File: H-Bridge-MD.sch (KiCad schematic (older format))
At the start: 69 parts, among them IC1 SI8650AB-B-IS1, IC2 A3921KLPTR-T, IC3 SI8650AB-B-IS1, IC4 A3921KLPTR-T, J1 Conn_01x02, J2 Conn_01x03, J3 Conn_01x05, J4 Conn_01x02, J5 Bus_mechaken_PCIexpress_x16_1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, Q1 NVMFD5C446NT1G, Q2 NVMFD5C446NT1G, Q3 NVMFD5C446NT1G, Q4 NVMFD5C446NT1G, U1 LDL1117S33R_SOT223-4, U2 STM32F042K6Tx, U3 MCP2562-E-SN, U4 LDL1117S33TR_SOT223-4

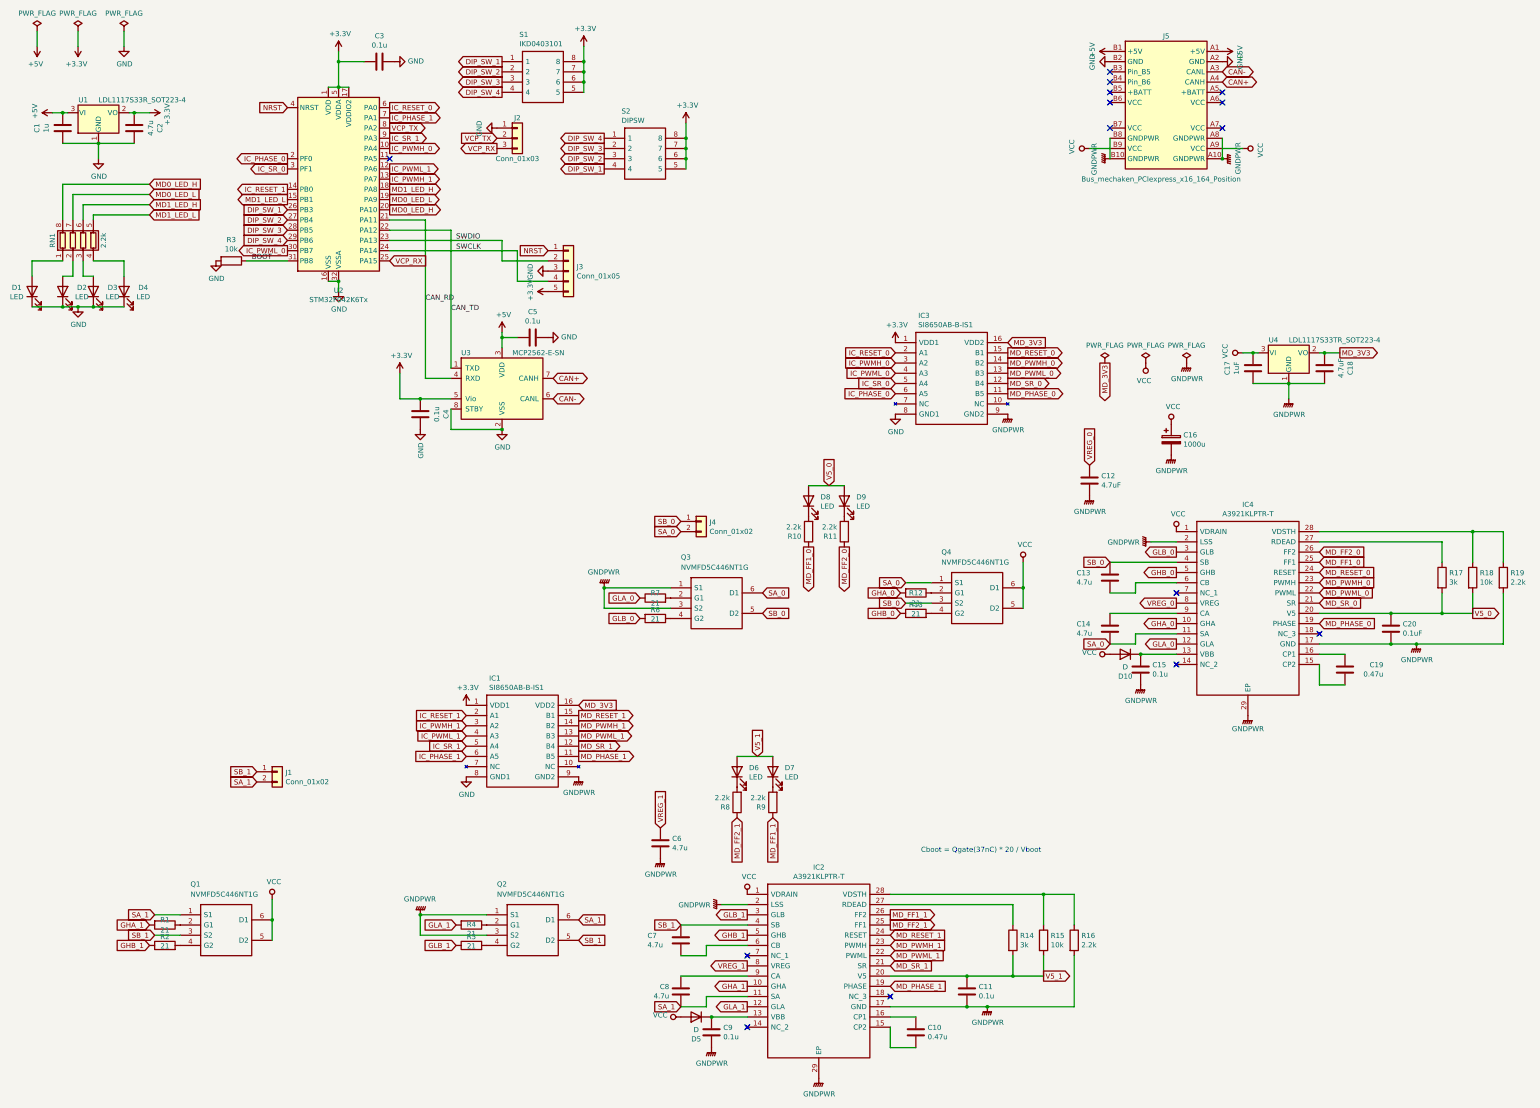
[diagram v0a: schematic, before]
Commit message: change
電源部のパスコンの追加
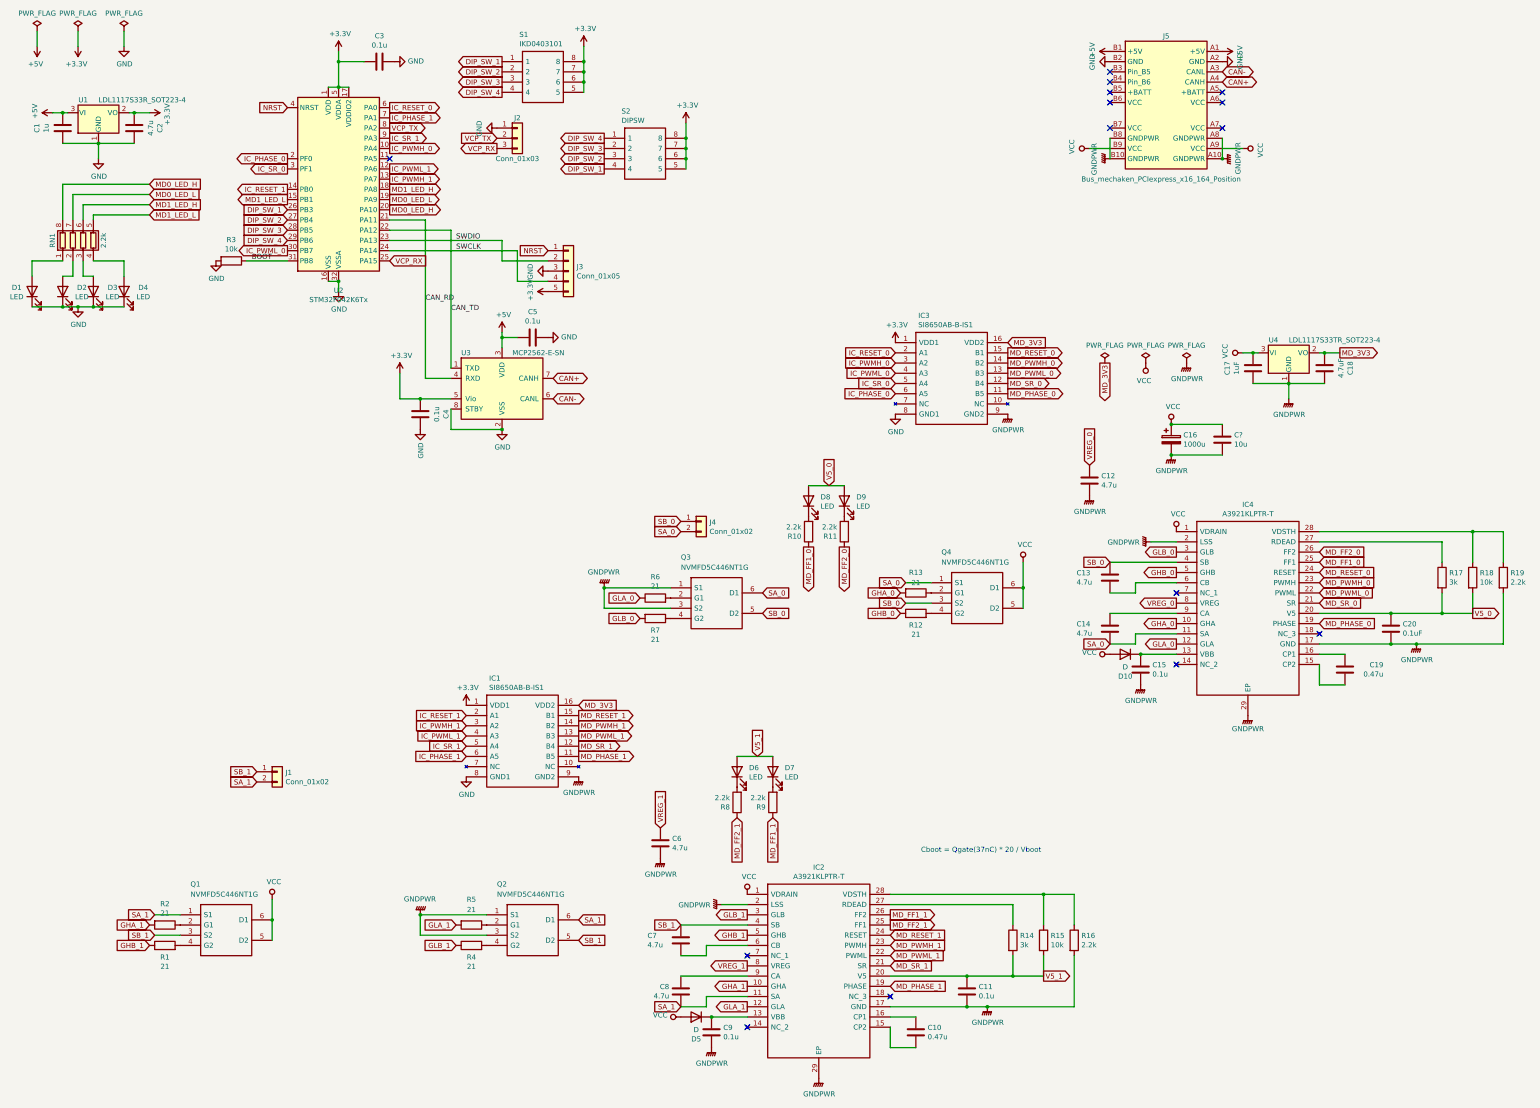
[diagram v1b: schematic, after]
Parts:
- added C?: 10u, Capacitor_SMD:C_0805_2012Metric, symbol Device:C
- C12: value 4.7uF -> 4.7u
- D10: footprint LED_SMD:LED_0603_1608Metric_Castellated -> Diode_SMD:D_0603_1608Metric
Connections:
- net GNDPWR: now also C?.2
- net VCC: now also C?.1
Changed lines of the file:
@@
 F 0 "D10" H 11400 7166 50  0000 C CNN
 F 1 "D" H 11400 7075 50  0000 C CNN
-F 2 "LED_SMD:LED_0603_1608Metric_Castellated" H 11400 6950 50  0001 C CNN
+F 2 "Diode_SMD:D_0603_1608Metric" H 11400 6950 50  0001 C CNN
 F 3 "~" H 11400 6950 50  0001 C CNN
 	1    11400 6950
@@
 U 1 1 5DA97C08
 P 2000 9600
-F 0 "R2" V 2115 9600 50  0000 C CNN
-F 1 "21" V 2206 9600 50  0000 C CNN
+F 0 "R2" V 1793 9600 50  0000 C CNN
+F 1 "21" V 1884 9600 50  0000 C CNN
 F 2 "Resistor_SMD:R_0603_1608Metric" V 1930 9600 50  0001 C CNN
 F 3 "~" H 2000 9600 50  0001 C CNN
@@
 U 1 1 5DA97BF0
 P 2000 9800
-F 0 "R1" V 2250 9800 50  0000 C CNN
-F 1 "21" V 2150 9800 50  0000 C CNN
+F 0 "R1" V 1885 9800 50  0000 C CNN
+F 1 "21" V 1794 9800 50  0000 C CNN
 F 2 "Resistor_SMD:R_0603_1608Metric" V 1930 9800 50  0001 C CNN
 F 3 "~" H 2000 9800 50  0001 C CNN
@@
 U 1 1 5DC02421
 P 9350 6550
-F 0 "R12" V 9550 6550 50  0000 C CNN
-F 1 "21" V 9450 6550 50  0000 C CNN
+F 0 "R12" V 9235 6550 50  0000 C CNN
+F 1 "21" V 9144 6550 50  0000 C CNN
 F 2 "Resistor_SMD:R_0603_1608Metric" V 9280 6550 50  0001 C CNN
 F 3 "~" H 9350 6550 50  0001 C CNN
@@
 U 1 1 5DC02427
 P 9350 6350
-F 0 "R13" V 9465 6350 50  0000 C CNN
-F 1 "21" V 9556 6350 50  0000 C CNN
+F 0 "R13" V 9150 6350 50  0000 C CNN
+F 1 "21" V 9250 6350 50  0000 C CNN
 F 2 "Resistor_SMD:R_0603_1608Metric" V 9280 6350 50  0001 C CNN
 F 3 "~" H 9350 6350 50  0001 C CNN
@@
 P 11050 5250
 F 0 "C12" H 11165 5296 50  0000 L CNN
-F 1 "4.7uF" H 11165 5205 50  0000 L CNN
+F 1 "4.7u" H 11165 5205 50  0000 L CNN
 F 2 "Capacitor_SMD:C_0805_2012Metric" H 11088 5100 50  0001 C CNN
 F 3 "~" H 11050 5250 50  0001 C CNN
@@
 U 1 1 5DC02488
 P 6800 6600
-F 0 "R7" V 6550 6600 50  0000 C CNN
-F 1 "21" V 6650 6600 50  0000 C CNN
+F 0 "R7" V 6915 6600 50  0000 C CNN
+F 1 "21" V 7006 6600 50  0000 C CNN
 F 2 "Resistor_SMD:R_0603_1608Metric" V 6730 6600 50  0001 C CNN
 F 3 "~" H 6800 6600 50  0001 C CNN
@@
 U 1 1 5DC0241B
 P 6800 6400
-F 0 "R6" V 6685 6400 50  0000 C CNN
-F 1 "21" V 6594 6400 50  0000 C CNN
+F 0 "R6" V 7007 6400 50  0000 C CNN
+F 1 "21" V 6916 6400 50  0000 C CNN
 F 2 "Resistor_SMD:R_0603_1608Metric" V 6730 6400 50  0001 C CNN
 F 3 "~" H 6800 6400 50  0001 C CNN
@@
 U 1 1 5DA97C02
 P 5000 9600
-F 0 "R5" V 5115 9600 50  0000 C CNN
-F 1 "21" V 5206 9600 50  0000 C CNN
+F 0 "R5" V 4750 9600 50  0000 C CNN
+F 1 "21" V 4850 9600 50  0000 C CNN
 F 2 "Resistor_SMD:R_0603_1608Metric" V 4930 9600 50  0001 C CNN
 F 3 "~" H 5000 9600 50  0001 C CNN
@@
 U 1 1 5DA97BEA
 P 5000 9800
-F 0 "R4" V 5207 9800 50  0000 C CNN
-F 1 "21" V 5116 9800 50  0000 C CNN
+F 0 "R4" V 4885 9800 50  0000 C CNN
+F 1 "21" V 4794 9800 50  0000 C CNN
 F 2 "Resistor_SMD:R_0603_1608Metric" V 4930 9800 50  0001 C CNN
 F 3 "~" H 5000 9800 50  0001 C CNN
@@
 	0    -1   -1   0
 $EndComp
+$Comp
+L Device:C C?
+U 1 1 5E1E4833
+P 12350 4850
+F 0 "C?" H 12465 4896 50  0000 L CNN
+F 1 "10u" H 12465 4805 50  0000 L CNN
+F 2 "Capacitor_SMD:C_0805_2012Metric" H 12388 4700 50  0001 C CNN
+F 3 "~" H 12350 4850 50  0001 C CNN
+	1    12350 4850
+	1    0    0    -1
+$EndComp
+Wire Wire Line
+	11850 4700 12350 4700
+Connection ~ 11850 4700
+Wire Wire Line
+	11850 5000 12350 5000
+Connection ~ 11850 5000
 $EndSCHEMATC

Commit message: fix
Motor0側にあるA3921のVCCにつながるビアを増加
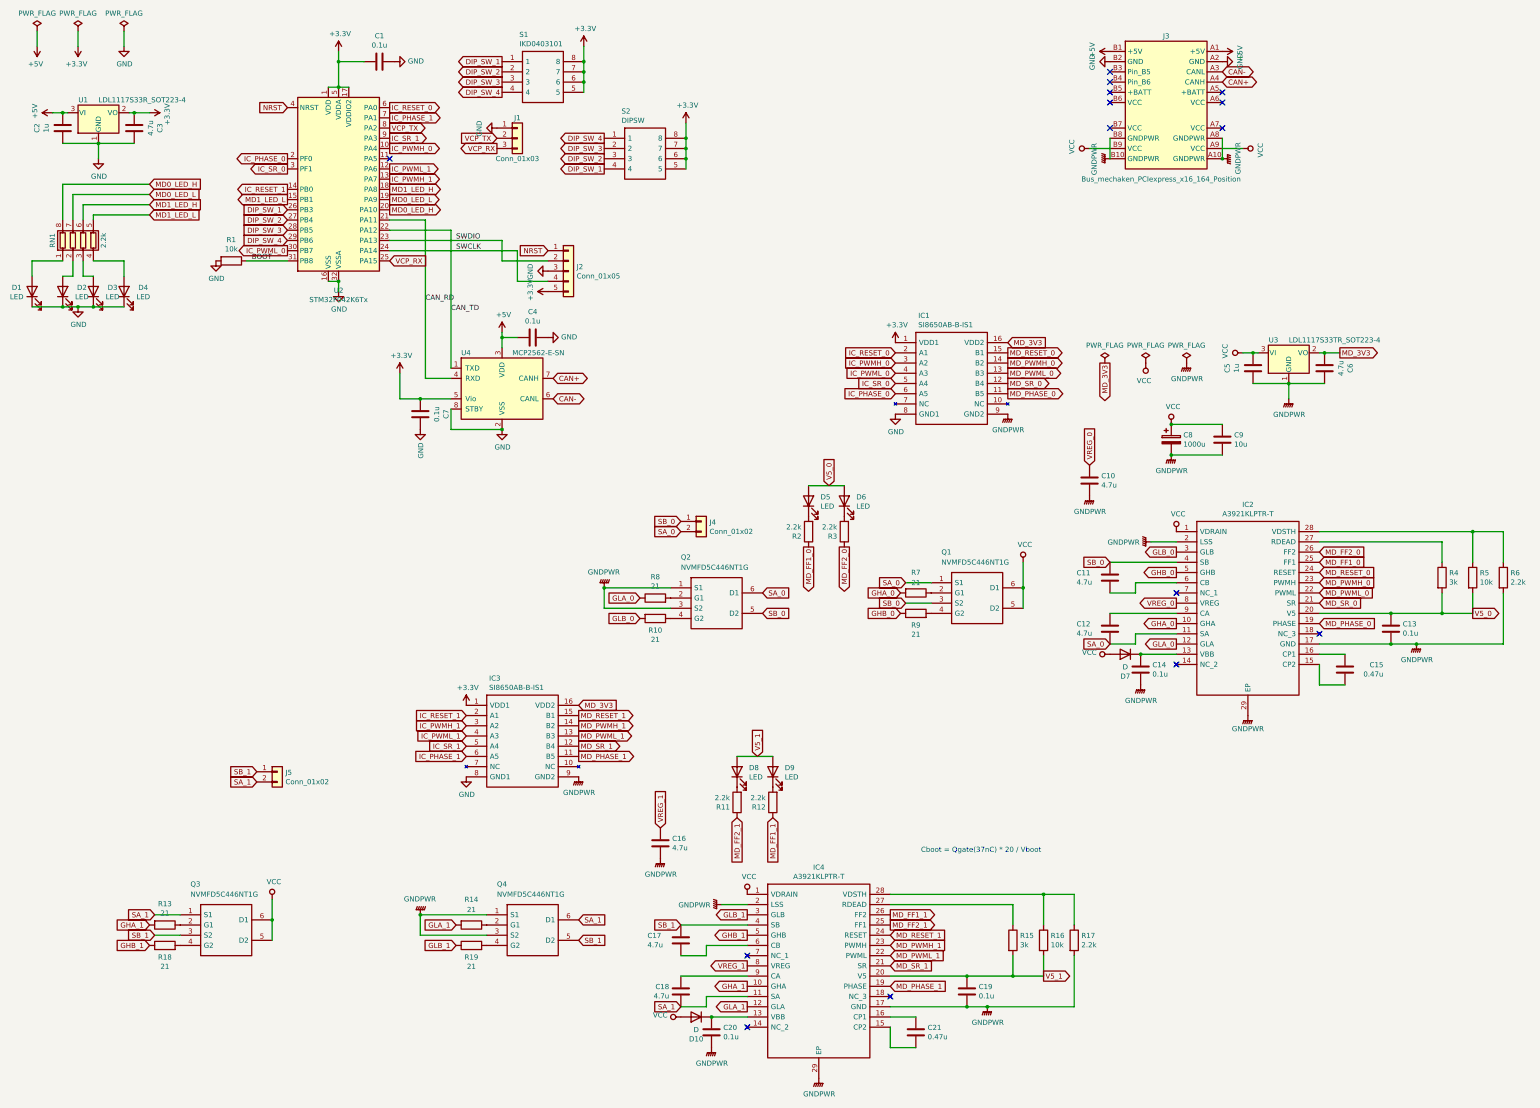
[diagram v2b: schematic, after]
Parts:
- C13: renamed from C20; value 0.1uF -> 0.1u
- C5: renamed from C17; value 1uF -> 1u
- C6: renamed from C18; value 4.7uF -> 4.7u
- gave numbers to parts that had none: 1
- renumbered C3 to C1, C12 to C10, C13 to C11, C14 to C12, C15 to C14, C19 to C15, C6 to C16, C7 to C17, C8 to C18, C11 to C19, C1 to C2, C9 to C20, C10 to C21, C2 to C3, C5 to C4, C4 to C7, C16 to C8, D5 to D10, D8 to D5, D9 to D6, D10 to D7, D6 to D8, D7 to D9, IC3 to IC1, IC4 to IC2, IC1 to IC3, IC2 to IC4, J2 to J1, J3 to J2, J5 to J3, J1 to J5, Q4 to Q1, Q3 to Q2, Q1 to Q3, Q2 to Q4, R3 to R1, R7 to R10, R8 to R11, R9 to R12, R2 to R13, R5 to R14, R14 to R15, R15 to R16, R16 to R17, R1 to R18, R4 to R19, R10 to R2, R11 to R3, R17 to R4, R18 to R5, R19 to R6, R13 to R7, R6 to R8, R12 to R9, U4 to U3, U3 to U4

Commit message: change LDO
アイソレータ用のLDOを変更
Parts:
- removed U3: LDL1117S33TR_SOT223-4, Package_TO_SOT_SMD:SOT-223-3_TabPin2, symbol H-Bridge-MD-rescue:LD1117S33TR_SOT223-Regulator_Linear
- added IC2: AP7381-50SA-7, SOT96P240X105-3N, symbol SamacSys_Parts:AP7381-50SA-7
- C6: value 4.7u -> 2.2u
- renumbered IC2 to IC3, IC3 to IC4, IC4 to IC5, U4 to U3
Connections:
- net GNDPWR: now also IC2.3 (GND)
- net MD_3V3: now also IC2.2 (VOUT)
- net VCC: now also IC2.1 (VIN)
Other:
- moved on the sheet: C5, C6
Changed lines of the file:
@@
 NoConn ~ 11900 7050
 $Comp
-L SamacSys_Parts:A3921KLPTR-T IC2
+L SamacSys_Parts:A3921KLPTR-T IC3
 U 1 1 5DC023BF
 P 11900 5750
-F 0 "IC2" H 12600 6015 50  0000 C CNN
+F 0 "IC3" H 12600 6015 50  0000 C CNN
 F 1 "A3921KLPTR-T" H 12600 5924 50  0000 C CNN
 F 2 "SamacSys_Parts:SOP65P640X120-29N" H 13150 5850 50  0001 L CNN
@@
 $EndComp
 $Comp
-L SamacSys_Parts:SI8650AB-B-IS1 IC3
+L SamacSys_Parts:SI8650AB-B-IS1 IC4
 U 1 1 5DAFE258
 P 4950 7450
-F 0 "IC3" H 5173 7715 50  0000 L CNN
+F 0 "IC4" H 5173 7715 50  0000 L CNN
 F 1 "SI8650AB-B-IS1" H 5173 7624 50  0000 L CNN
 F 2 "SamacSys_Parts:SOIC127P600X175-16N" H 5900 7550 50  0001 L CNN
@@
 NoConn ~ 7700 10600
 $Comp
-L SamacSys_Parts:A3921KLPTR-T IC4
+L SamacSys_Parts:A3921KLPTR-T IC5
 U 1 1 5DA97B5E
 P 7700 9300
-F 0 "IC4" H 8400 9565 50  0000 C CNN
+F 0 "IC5" H 8400 9565 50  0000 C CNN
 F 1 "A3921KLPTR-T" H 8400 9474 50  0000 C CNN
 F 2 "SamacSys_Parts:SOP65P640X120-29N" H 8950 9400 50  0001 L CNN
@@
 Text GLabel 7600 8550 3    50   Input ~ 0
 MD_FF2_1
-Text GLabel 13500 4000 2    50   Output ~ 0
+Text GLabel 12750 4150 0    50   Output ~ 0
 MD_3V3
 Text Label 4800 3600 0    50   ~ 0
@@
 Connection ~ 6300 6300
 $Comp
-L Interface_CAN_LIN:MCP2562-E-SN U4
+L Interface_CAN_LIN:MCP2562-E-SN U3
 U 1 1 5DB5AF60
 P 5300 4350
-F 0 "U4" H 4900 4700 50  0000 L CNN
+F 0 "U3" H 4900 4700 50  0000 L CNN
 F 1 "MCP2562-E-SN" H 5400 4700 50  0000 L CNN
 F 2 "Package_SO:SOIC-8_3.9x4.9mm_P1.27mm" H 5300 3850 50  0001 C CIN
@@
 Wire Wire Line
 	10400 6300 10400 6500
-Wire Wire Line
-	12650 4000 12700 4000
-Connection ~ 12650 4000
-Wire Wire Line
-	13350 4000 13500 4000
-Connection ~ 13350 4000
-Wire Wire Line
-	13350 4300 13000 4300
-Wire Wire Line
-	13000 4300 12650 4300
-Connection ~ 13000 4300
-Wire Wire Line
-	13000 4300 13000 4450
-Wire Wire Line
-	13300 4000 13350 4000
-Wire Wire Line
-	12550 4000 12650 4000
-$Comp
-L Device:C C5
-U 1 1 5DF18189
-P 12650 4150
-F 0 "C5" V 12398 4150 50  0000 C CNN
-F 1 "1u" V 12489 4150 50  0000 C CNN
-F 2 "Capacitor_SMD:C_0805_2012Metric" H 12688 4000 50  0001 C CNN
-F 3 "~" H 12650 4150 50  0001 C CNN
-	1    12650 4150
-	1    0    0    -1
-$EndComp
 $Comp
 L Device:C C6
 U 1 1 5DF1818F
-P 13350 4150
-F 0 "C6" V 13098 4150 50  0000 C CNN
-F 1 "4.7u" V 13189 4150 50  0000 C CNN
-F 2 "Capacitor_SMD:C_0805_2012Metric" H 13388 4000 50  0001 C CNN
-F 3 "~" H 13350 4150 50  0001 C CNN
-	1    13350 4150
+P 12800 4300
+F 0 "C6" H 12915 4254 50  0000 L CNN
+F 1 "2.2u" H 12915 4345 50  0000 L CNN
+F 2 "Capacitor_SMD:C_0805_2012Metric" H 12838 4150 50  0001 C CNN
+F 3 "~" H 12800 4300 50  0001 C CNN
+	1    12800 4300
 	-1   0    0    1
-$EndComp
-$Comp
-L H-Bridge-MD-rescue:LD1117S33TR_SOT223-Regulator_Linear U3
-U 1 1 5DF181A7
-P 13000 4000
-F 0 "U3" H 12850 4125 50  0000 C CNN
-F 1 "LDL1117S33TR_SOT223-4" H 13000 4125 50  0000 L CNN
-F 2 "Package_TO_SOT_SMD:SOT-223-3_TabPin2" H 13000 4200 50  0001 C CNN
-F 3 "http://www.st.com/st-web-ui/static/active/en/resource/technical/document/datasheet/CD00000544.pdf" H 13100 3750 50  0001 C CNN
-	1    13000 4000
-	1    0    0    -1
 $EndComp
 $Comp
 L power:VCC #PWR028
 U 1 1 5DF2B13A
-P 12550 4000
-F 0 "#PWR028" H 12550 3850 50  0001 C CNN
-F 1 "VCC" H 12567 4173 50  0000 C CNN
-F 2 "" H 12550 4000 50  0001 C CNN
-F 3 "" H 12550 4000 50  0001 C CNN
-	1    12550 4000
+P 13000 4050
+F 0 "#PWR028" H 13000 3900 50  0001 C CNN
+F 1 "VCC" H 13017 4223 50  0000 C CNN
+F 2 "" H 13000 4050 50  0001 C CNN
+F 3 "" H 13000 4050 50  0001 C CNN
+	1    13000 4050
 	0    -1   -1   0
 $EndComp
@@
 L power:GNDPWR #PWR032
 U 1 1 5DFADA6B
-P 13000 4450
-F 0 "#PWR032" H 13000 4250 50  0001 C CNN
-F 1 "GNDPWR" H 13004 4296 50  0000 C CNN
-F 2 "" H 13000 4400 50  0001 C CNN
-F 3 "" H 13000 4400 50  0001 C CNN
-	1    13000 4450
+P 14400 4450
+F 0 "#PWR032" H 14400 4250 50  0001 C CNN
+F 1 "GNDPWR" H 14404 4296 50  0000 C CNN
+F 2 "" H 14400 4400 50  0001 C CNN
+F 3 "" H 14400 4400 50  0001 C CNN
+	1    14400 4450
 	1    0    0    -1
 $EndComp
@@
 	11850 5000 12350 5000
 Connection ~ 11850 5000
+$Comp
+L SamacSys_Parts:AP7381-50SA-7 IC2
+U 1 1 5E271866
+P 13300 4050
+F 0 "IC2" H 13850 4315 50  0000 C CNN
+F 1 "AP7381-50SA-7" H 13850 4224 50  0000 C CNN
+F 2 "SOT96P240X105-3N" H 14250 4150 50  0001 L CNN
+F 3 "https://componentsearchengine.com/Datasheets/1/AP7381-50SA-7.pdf" H 14250 4050 50  0001 L CNN
+F 4 "LDO Voltage Regulators LDO CMOS LowCurr SOT23 T&R 3K" H 14250 3950 50  0001 L CNN "Description"
+F 5 "1.05" H 14250 3850 50  0001 L CNN "Height"
+F 6 "621-AP7381-50SA-7" H 14250 3750 50  0001 L CNN "Mouser Part Number"
+F 7 "https://www.mouser.com/Search/Refine.aspx?Keyword=621-AP7381-50SA-7" H 14250 3650 50  0001 L CNN "Mouser Price/Stock"
+F 8 "Diodes Inc." H 14250 3550 50  0001 L CNN "Manufacturer_Name"
+F 9 "AP7381-50SA-7" H 14250 3450 50  0001 L CNN "Manufacturer_Part_Number"
+	1    13300 4050
+	1    0    0    -1
+$EndComp
+$Comp
+L Device:C C5
+U 1 1 5DF18189
+P 13100 4200
+F 0 "C5" H 13215 4246 50  0000 L CNN
+F 1 "1u" H 13215 4155 50  0000 L CNN
+F 2 "Capacitor_SMD:C_0805_2012Metric" H 13138 4050 50  0001 C CNN
+F 3 "~" H 13100 4200 50  0001 C CNN
+	1    13100 4200
+	1    0    0    -1
+$EndComp
+Wire Wire Line
+	13300 4050 13100 4050
+Connection ~ 13100 4050
+Wire Wire Line
+	13100 4050 13000 4050
+Wire Wire Line
+	12750 4150 12800 4150
+Connection ~ 12800 4150
+Wire Wire Line
+	12800 4150 13300 4150
+Wire Wire Line
+	12800 4450 13100 4450
+Wire Wire Line
+	13100 4350 13100 4450
+Connection ~ 13100 4450
+Wire Wire Line
+	13100 4450 14400 4450
+Wire Wire Line
+	14400 4450 14400 4050
+Connection ~ 14400 4450
 $EndSCHEMATC

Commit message: change
エッジコネクタ（PCIe）を公式のライブラリを基にしたフットプリントに変更
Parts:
- IC2: footprint SOT96P240X105-3N -> SamacSys_Parts:SOT96P240X105-3N
- J3: footprint PCIe:BUS_mechaken_PCIexpress_x16_164_Position -> PCIe:BUS_mechaken_PCIexpress_x16
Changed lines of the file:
@@
 F 0 "J3" H 11800 7100 50  0000 C CNN
 F 1 "Bus_mechaken_PCIexpress_x16_164_Position" H 11750 5700 50  0000 C CNN
-F 2 "PCIe:BUS_mechaken_PCIexpress_x16_164_Position" H 11450 3900 50  0001 C CNN
+F 2 "PCIe:BUS_mechaken_PCIexpress_x16" H 11450 3900 50  0001 C CNN
 F 3 "http://pinouts.ru/Slots/PCI_pinout.shtml" H 11450 3900 50  0001 C CNN
 	1    11800 4000
@@
 F 0 "IC2" H 13850 4315 50  0000 C CNN
 F 1 "AP7381-50SA-7" H 13850 4224 50  0000 C CNN
-F 2 "SOT96P240X105-3N" H 14250 4150 50  0001 L CNN
+F 2 "SamacSys_Parts:SOT96P240X105-3N" H 14250 4150 50  0001 L CNN
 F 3 "https://componentsearchengine.com/Datasheets/1/AP7381-50SA-7.pdf" H 14250 4050 50  0001 L CNN
 F 4 "LDO Voltage Regulators LDO CMOS LowCurr SOT23 T&R 3K" H 14250 3950 50  0001 L CNN "Description"
